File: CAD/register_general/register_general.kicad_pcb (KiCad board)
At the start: 2 copper layers, 75 x 28 mm, 42 parts, among them J1 Conn_01x16_Pin, J2 Conn_01x16_Pin, U1 74HC245, U2 74HC377

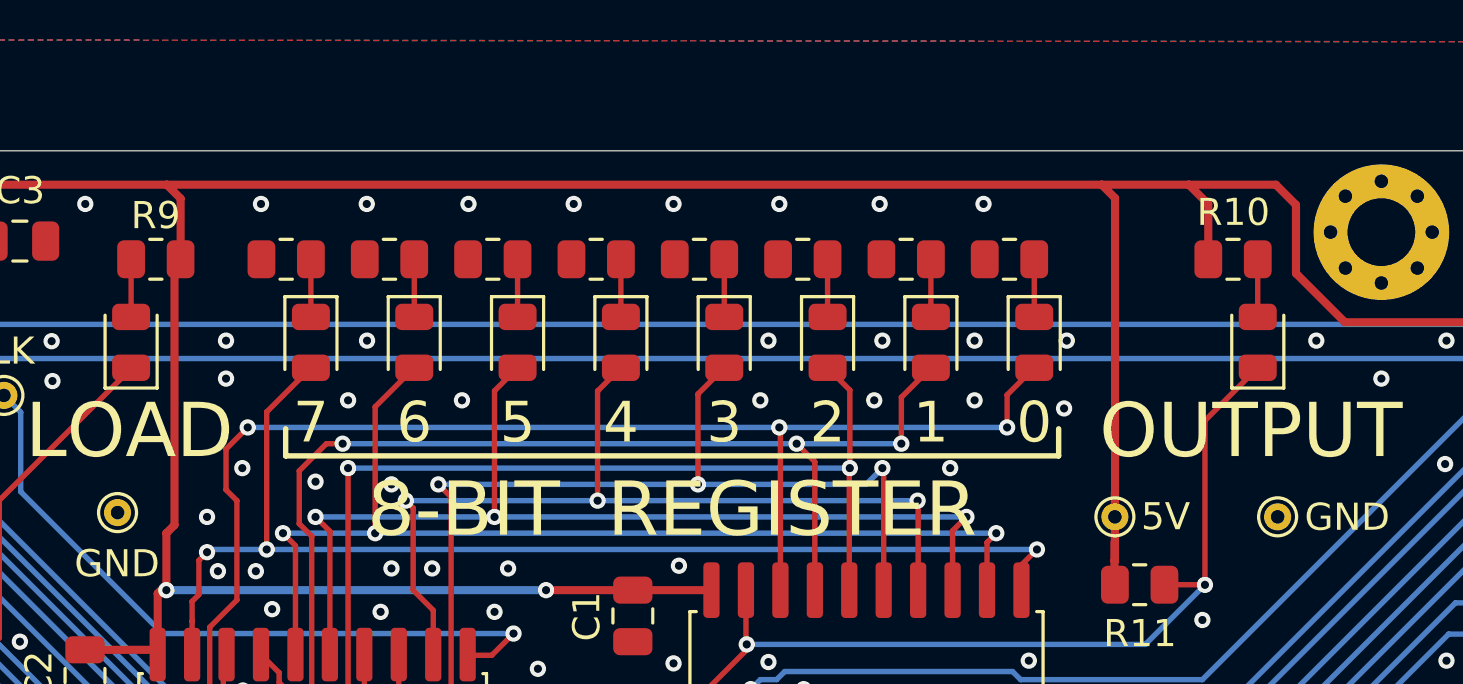
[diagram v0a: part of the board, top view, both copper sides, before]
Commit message: add slotted test point for 5V to general register
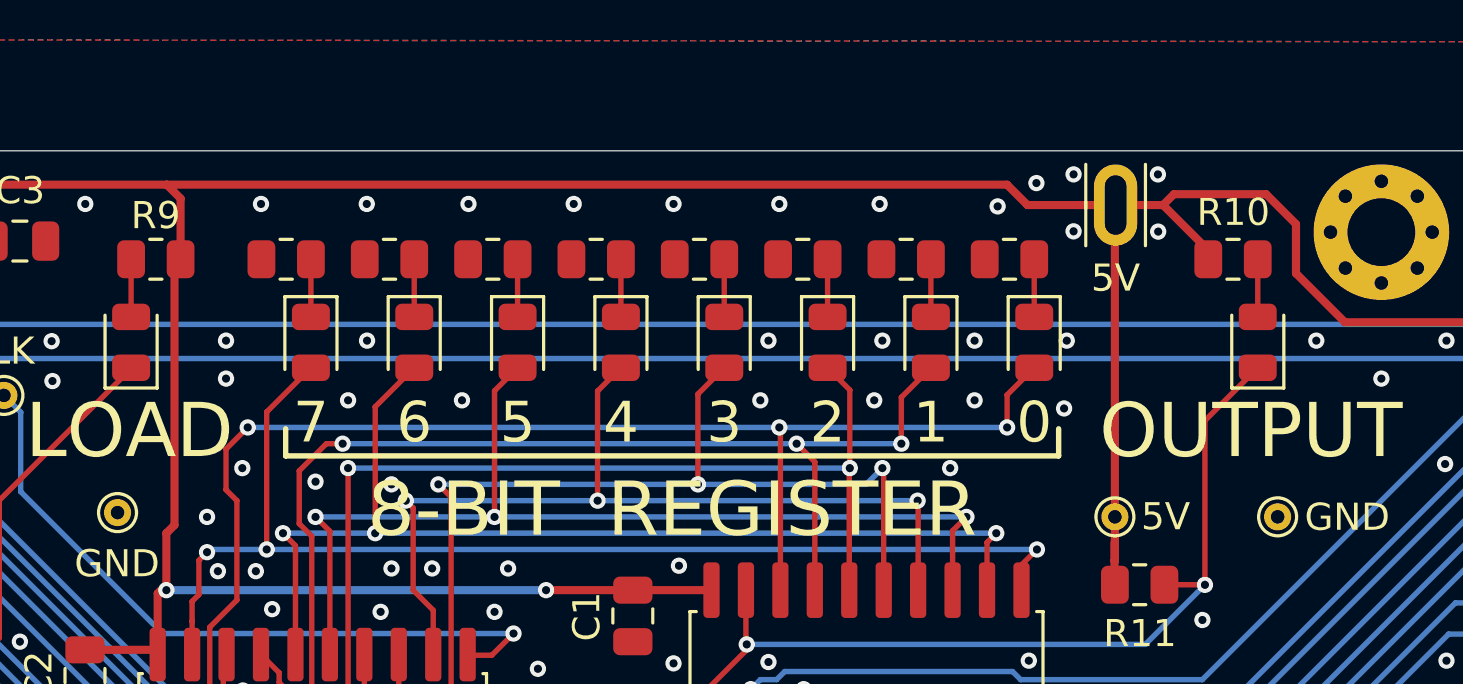
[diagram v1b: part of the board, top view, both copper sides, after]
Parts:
- added TP5: TestPoint, 8-bit_computer:TestPoint_Slot_2.2x0.8mm, F.Cu at (129.3, 66.0)
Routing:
- net +5V: track 154.8 -> 152.7 mm
- net GND: vias 73 -> 78

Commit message: update KiCAD version 10.0
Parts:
- removed G***: LOGO, 8-bit_computer:qr-code-github
